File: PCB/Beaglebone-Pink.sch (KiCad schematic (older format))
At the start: 0 parts

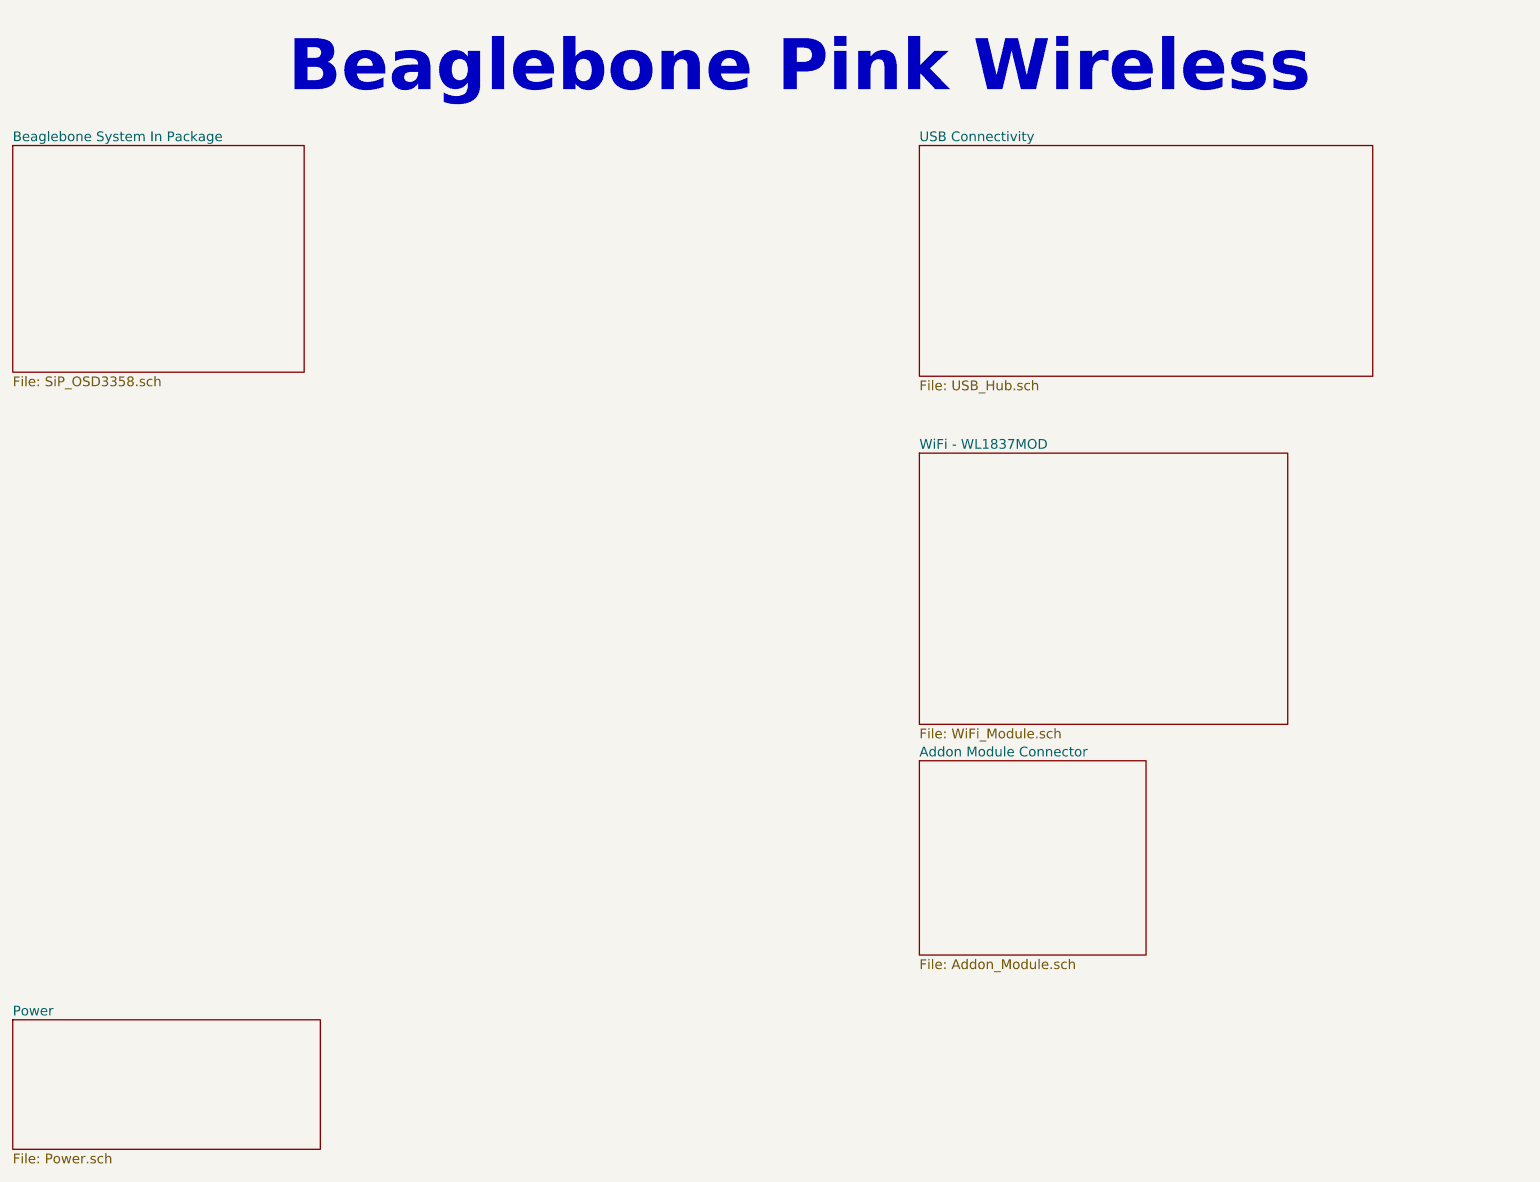
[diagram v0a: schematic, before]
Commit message: Spec Changes and Schematic
Tiny bit of progress on the schematic and change to the feature set. The
sub 1GHZ radio is going to be integrated into the same board as the
beagle sip, I'm doing away with the USB hub for now. Doing away with the
wireless chip from Ti going to use a ESP32 as a realtime controller and
for standard wireless since the focus is remote wireless not indoor
wireless. Need to fit all the important stuff first before adding extra
features like a USB hub.
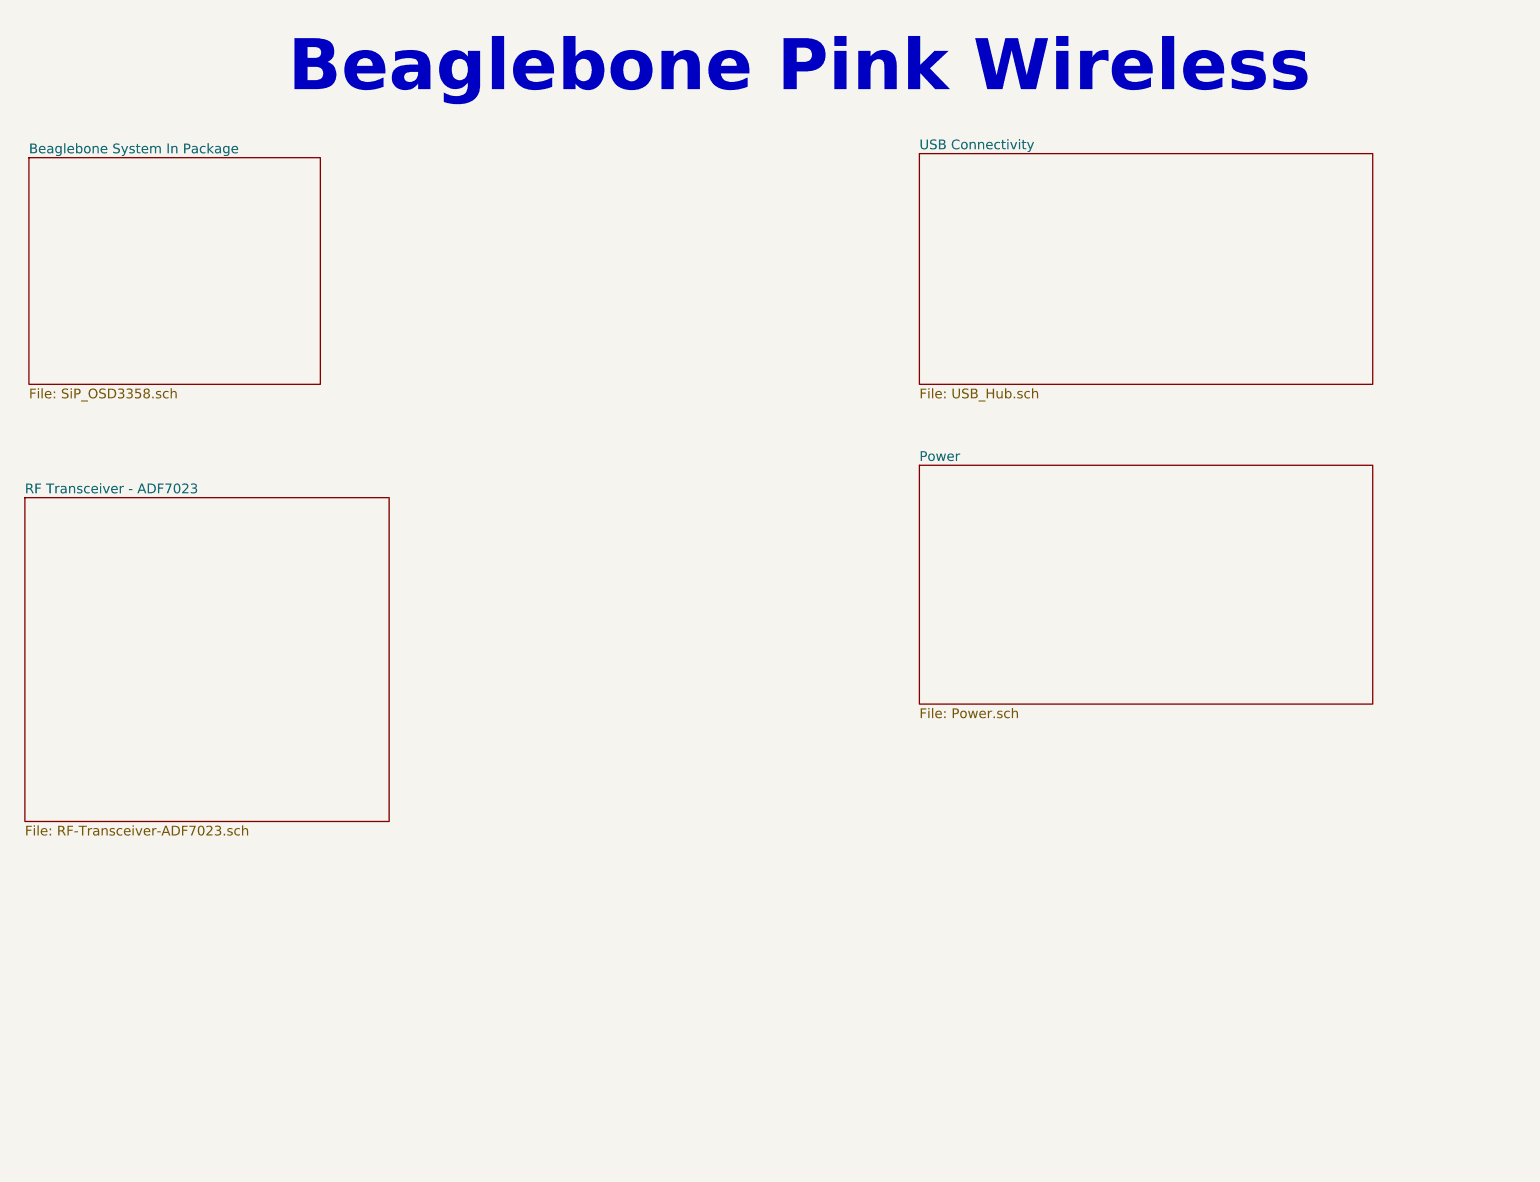
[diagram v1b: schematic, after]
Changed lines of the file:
@@
 LIBS:valves
 LIBS:OSD335x
-LIBS:kicad-library_2
 LIBS:Beaglebone-Pink-Lib
+LIBS:HydroPWNics_Lib
 LIBS:Beaglebone-Pink-cache
-EELAYER 25 0
+EELAYER 26 0
 EELAYER END
 $Descr A4 11693 8268
 encoding utf-8
-Sheet 1 6
+Sheet 1 5
 Title ""
 Date "2016-10-16"
@@
 Beaglebone Pink Wireless
 $Sheet
-S 1400 6800 1900 800
+S 7000 3375 2800 1475
 U 58040242
 F0 "Power" 60
@@
 $EndSheet
 $Sheet
-S 7000 3300 2275 1675
-U 58040262
-F0 "WiFi - WL1837MOD" 60
-F1 "WiFi_Module.sch" 60
+S 1500 1475 1800 1400
+U 5804022F
+F0 "Beaglebone System In Package" 60
+F1 "SiP_OSD3358.sch" 60
 $EndSheet
 $Sheet
-S 7000 1400 2800 1425
+S 7000 1450 2800 1425
 U 580402EF
 F0 "USB Connectivity" 60
@@
 $EndSheet
 $Sheet
-S 7000 5200 1400 1200
-U 58040393
-F0 "Addon Module Connector" 60
-F1 "Addon_Module.sch" 60
-$EndSheet
-$Sheet
-S 1400 1400 1800 1400
-U 5804022F
-F0 "Beaglebone System In Package" 60
-F1 "SiP_OSD3358.sch" 60
+S 1475 3575 2250 2000
+U 5882F261
+F0 "RF Transceiver - ADF7023" 60
+F1 "RF-Transceiver-ADF7023.sch" 60
 $EndSheet
 $EndSCHEMATC
